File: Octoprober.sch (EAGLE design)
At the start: 70 parts, among them J1 10118193-0001LF, P1 TC33X-1, SW1 101-0134-EV, U1 P8X32A-M44, U10 MAX31855KASA+, U11 MAX31855KASA+, U12 MAX31855KASA+, U13 MAX31855KASA+, U14 MAX31855KASA+, U2 CAT24C512WI-GT3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

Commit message: Added lithium battery. Still need to add charger.
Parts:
- removed R14: 1K, PP_Passives:RESISTOR0402
- removed U5: TPS2115ADRBR, PP_PowerIC:TPS2115SON-8
- added BATT1: 1042, PP_Connectors:LI-ION_18650_HOLDER1042
- U3: value TS2937CW33 -> ADP3338AKCZ-3.3-RL; device PP_PowerIC:FIXED_VOLTAGE_REGSOT-223 -> PP_PowerIC:FIXED_VOLTAGE_REGSOT-223_ALT
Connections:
- removed net 5V: C7.1, C9.1, U3.IN, U5.OUT
- removed net ILIM: R14.1, U5.ILIM
- removed net VBUS_2: U5.IN2
- net 3.3V: no longer R13.1
- net GND: now also BATT1.-; no longer R14.2, U5.D1, U5.GND
- net VBATT: now also BATT1.+, C7.1, C9.1, U3.IN; no longer U5.IN1
- net VBUS_P1: no longer R12.1
- net VBUS_P2: now also R12.1, R13.1

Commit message: Added BQ24075RGTT for charging.
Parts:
- added C31, C32, C33: 10uF, PP_Passives:CAPACITOR_NON_POLAR1206
- added R14, R19, R20: 10K, PP_Passives:RESISTOR0402
- added R17: 1.18K, PP_Passives:RESISTOR0402
- added R18: 1.13K, PP_Passives:RESISTOR0402
- added U5: BQ24075RGTT, PP_PowerIC:BQ2407XQFN-16
- R15: value 100K -> 10K
- R16: value 1K -> 10K
- U6: value IRLML6401TRPBF -> 74HC2G04GV,125; device PP_DiscreteSemi:MOSFET_P-CHANNEL_SINGLESOT-23 -> PP_DigitalIC:74HCT2G04GV,125TTSOP-6
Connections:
- net VBUS renamed USB_V0
- removed net P19: U1.P19
- removed net P20: U1.P20
- removed net PWREN_GATE: R15.2, R16.2, U6.GATE
- removed net VBUS_P1: C13.1, C14.1, L1.2, R15.1, U4.VCC, U6.SOURCE
- removed net VBUS_P2: R12.1, R13.1, U6.DRAIN
- new net !PWREN: U5.EN1, U6.2Y
- new net !SLEEP: U1.P20, U5.!CE, U6.1Y
- new net BCD_CHARGER: R20.2, U4.CBUS2, U5.EN2
- new net CHARGING: R15.2, U1.P19, U5.!CHG
- new net ILM: R17.1, U5.ILM
- new net ISET: R18.1, U5.ISET
- new net PGOOD: R16.2, U5.!PGOOD
- new net SLEEP: U4.CBUS1, U6.1A
- new net SYS_V: C32.1, C7.1, C9.1, U3.IN, U5.OUT
- new net TS: R14.1, U5.TS
- new net USB_V1: C13.1, C14.1, C33.1, L1.2, R12.1, R13.1, U4.VCC, U5.IN
- net 3.3V: now also R15.1, R16.1, R19.2, U6.VCC
- net GND: now also C31.2, C32.2, C33.2, R14.2, R17.2, R18.2, R20.1, U5.SYSOFF, U5.VSS, U6.GND
- net PWREN: now also R19.1, U6.2A; no longer R16.1
- net TXRX_LED: now also U4.CBUS0; no longer U4.CBUS2
- net VBATT: now also C31.1, U5.BAT; no longer C7.1, C9.1, U3.IN
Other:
- moved on the sheet: BATT1, R15, R16

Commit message: Still need Battery Monitoring Solution
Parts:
- added U15: BSS138, PP_DiscreteSemi:MOSFET_N-CHANNEL_SINGLESOT-23
- LCD1: device PP_Displays:CHAR_DISPLAY1602_4_HOLE -> PP_Displays:HD44780_LCD1602_COUNTERSINK
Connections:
- removed net N$38: LCD1.BK_V
- removed net N$39: LCD1.BK_GND
- removed net P21: U1.P21
- new net BK_GATE: U1.P21, U15.GATE
- new net BK_GND: LCD1.BK_GND, U15.DRAIN
- new net SYS_V_SW: C7.1, C9.1, U3.IN
- net !PWREN: now also R19.1, U4.CBUS3, U6.2A; no longer U5.EN1, U6.2Y
- net !SLEEP: now also U4.CBUS1, U6.1A; no longer U5.!CE, U6.1Y
- net 3.3V: now also LCD1.BK_V
- net GND: now also U15.SOURCE
- net PWREN: now also U5.EN1, U6.2Y; no longer R19.1, U4.CBUS3, U6.2A
- net SLEEP: now also U5.!CE, U6.1Y; no longer U4.CBUS1, U6.1A
- net SYS_V: no longer C7.1, C9.1, U3.IN
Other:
- moved on the sheet: BATT1, C10, C2, C3, C31, C32, C33, C4, C5, C6, C7, C8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

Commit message: Added Soft power switch
Soft power circuit to enable MCU to initiate a shutdown of the system to
prevent corruption of the SD Card.
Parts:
- added C34, C35: 0.1uF, PP_Passives:CAPACITOR_NON_POLAR0402
- added C36: 10uF, PP_Passives:CAPACITOR_NON_POLAR1206
- added D3: PMEG6030EP,115, PP_Passives:DIODESOD-128
- added R21, R22, R23, R25: 10K, PP_Passives:RESISTOR0402
- added R24, R26: 100K, PP_Passives:RESISTOR0402
- added R27: 300K, PP_Passives:RESISTOR0402
- added SW2, SW3, SW4, SW5: EVQ-Q2203W, PP_Electromechanical:SPSTEVQ-Q2203W
- added U16: PMV22EN,215, PP_DiscreteSemi:MOSFET_N-CHANNEL_SINGLESOT-23
- added U17: PMV160UP,215, PP_DiscreteSemi:MOSFET_P-CHANNEL_SINGLESOT-23
- SW1: value 101-0134-EV -> EVQ-Q2203W; device PP_Electromechanical:SPST101-0134-EV -> PP_Electromechanical:SPSTEVQ-Q2203W
- U15: value BSS138 -> PMV22EN,215
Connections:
- removed net P22: U1.P22
- removed net P23: U1.P23
- removed net P24: U1.P24
- removed net P25: U1.P25
- new net N$4: C35.1, D3.CATHODE, R25.1, SW5.B
- new net N$5: C36.2, R27.2, U16.GATE
- new net PWR_SW: D3.ANODE, R26.1, R27.1, U1.P25
- new net SW_DWN: R23.1, SW4.B, U1.P24
- new net SW_SEL: R22.1, SW3.B, U1.P23
- new net SW_UP: R21.1, SW2.B, U1.P22
- new net S_P_G: C34.2, C35.2, R24.1, U16.DRAIN, U17.GATE
- net 3.3V: now also C36.1, R21.2, R22.2, R23.2, R26.2
- net GND: now also SW2.A, SW3.A, SW4.A, SW5.A, U16.SOURCE
- net SYS_V: now also C34.1, R24.2, R25.2, U17.SOURCE
- net SYS_V_SW: now also U17.DRAIN
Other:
- moved on the sheet: J1

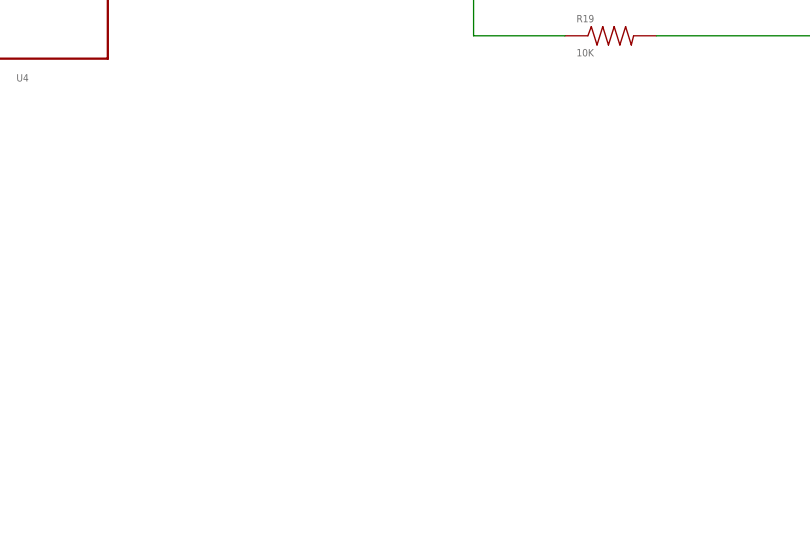
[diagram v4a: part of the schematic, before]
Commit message: Added ADC. Might use it for battery voltage level.
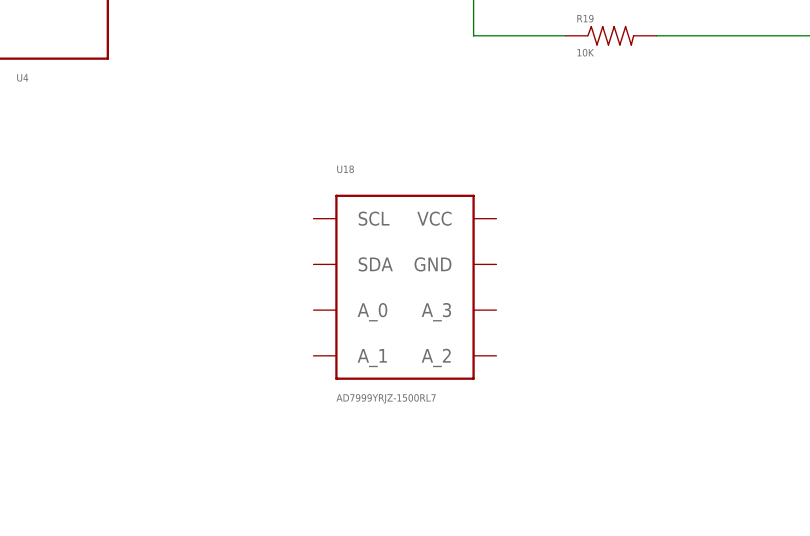
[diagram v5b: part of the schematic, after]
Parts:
- added U18: AD7999YRJZ-1500RL7, PP_DigitalIC:AD799XSOT-23-8
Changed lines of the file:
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@@
 <part name="R26" library="PP_Passives" deviceset="RESISTOR" device="0402" value="100K"/>
 <part name="R27" library="PP_Passives" deviceset="RESISTOR" device="0402" value="300K"/>
+<part name="U18" library="PP_DigitalIC" deviceset="AD799X" device="SOT-23-8" value="AD7999YRJZ-1500RL7"/>
 </parts>
 <sheets>
@@
 <instance part="R26" gate="G$1" x="139.7" y="-66.04" rot="R90"/>
 <instance part="R27" gate="G$1" x="132.08" y="-76.2" rot="R180"/>
+<instance part="U18" gate="G$1" x="-15.24" y="-101.6"/>
 </instances>
 <busses>

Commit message: Created Board. Still need to figure out connector
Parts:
- added U$2: OCTOPROBER_LOGONORMAL, PP_Aesthetics:OCTOPROBER_LOGONORMAL
- U1: device PP_DigitalIC:P8X32A_PROPELLERQFN-44 -> PP_DigitalIC:P8X32A_PROPELLERLQFP/QFN-44
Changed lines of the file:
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@@
 <grid distance="0.1" unitdist="inch" unit="inch" style="lines" multiple="1" display="no" altdistance="0.01" altunitdist="inch" altunit="inch"/>
 <layers>
-<layer number="1" name="Top" color="4" fill="1" visible="no" active="no"/>
-<layer number="16" name="Bottom" color="1" fill="1" visible="no" active="no"/>
-<layer number="17" name="Pads" color="2" fill="1" visible="no" active="no"/>
-<layer number="18" name="Vias" color="2" fill="1" visible="no" active="no"/>
-<layer number="19" name="Unrouted" color="6" fill="1" visible="no" active="no"/>
-<layer number="20" name="Dimension" color="15" fill="1" visible="no" active="no"/>
-<layer number="21" name="tPlace" color="7" fill="1" visible="no" active="no"/>
-<layer number="22" name="bPlace" color="7" fill="1" visible="no" active="no"/>
-<layer number="23" name="tOrigins" color="15" fill="1" visible="no" active="no"/>
-<layer number="24" name="bOrigins" color="15" fill="1" visible="no" active="no"/>
-<layer number="25" name="tNames" color="7" fill="1" visible="no" active="no"/>
-<layer number="26" name="bNames" color="7" fill="1" visible="no" active="no"/>
-<layer number="27" name="tValues" color="7" fill="1" visible="no" active="no"/>
-<layer number="28" name="bValues" color="7" fill="1" visible="no" active="no"/>
+<layer number="1" name="Top" color="4" fill="1" visible="yes" active="no"/>
+<layer number="16" name="Bottom" color="1" fill="1" visible="yes" active="no"/>
+<layer number="17" name="Pads" color="2" fill="1" visible="yes" active="no"/>
+<layer number="18" name="Vias" color="2" fill="1" visible="yes" active="no"/>
+<layer number="19" name="Unrouted" color="6" fill="1" visible="yes" active="no"/>
+<layer number="20" name="Dimension" color="15" fill="1" visible="yes" active="no"/>
+<layer number="21" name="tPlace" color="7" fill="1" visible="yes" active="no"/>
+<layer number="22" name="bPlace" color="7" fill="1" visible="yes" active="no"/>
+<layer number="23" name="tOrigins" color="15" fill="1" visible="yes" active="no"/>
+<layer number="24" name="bOrigins" color="15" fill="1" visible="yes" active="no"/>
+<layer number="25" name="tNames" color="7" fill="1" visible="yes" active="no"/>
+<layer number="26" name="bNames" color="7" fill="1" visible="yes" active="no"/>
+<layer number="27" name="tValues" color="7" fill="1" visible="yes" active="no"/>
+<layer number="28" name="bValues" color="7" fill="1" visible="yes" active="no"/>
 <layer number="29" name="tStop" color="7" fill="3" visible="no" active="no"/>
 <layer number="30" name="bStop" color="7" fill="6" visible="no" active="no"/>
@@
 <layer number="35" name="tGlue" color="7" fill="4" visible="no" active="no"/>
 <layer number="36" name="bGlue" color="7" fill="5" visible="no" active="no"/>
-<layer number="37" name="tTest" color="7" fill="1" visible="no" active="no"/>
-<layer number="38" name="bTest" color="7" fill="1" visible="no" active="no"/>
+<layer number="37" name="tTest" color="7" fill="1" visible="yes" active="no"/>
+<layer number="38" name="bTest" color="7" fill="1" visible="yes" active="no"/>
 <layer number="39" name="tKeepout" color="4" fill="11" visible="no" active="no"/>
 <layer number="40" name="bKeepout" color="1" fill="11" visible="no" active="no"/>
@@
 <layer number="44" name="Drills" color="7" fill="1" visible="no" active="no"/>
 <layer number="45" name="Holes" color="7" fill="1" visible="no" active="no"/>
-<layer number="46" name="Milling" color="3" fill="1" visible="no" active="no"/>
-<layer number="47" name="Measures" color="7" fill="1" visible="no" active="no"/>
-<layer number="48" name="Document" color="7" fill="1" visible="no" active="no"/>
-<layer number="49" name="Reference" color="7" fill="1" visible="no" active="no"/>
-<layer number="50" name="dxf" color="7" fill="1" visible="no" active="no"/>
-<layer number="51" name="tDocu" color="7" fill="1" visible="no" active="no"/>
-<layer number="52" name="bDocu" color="7" fill="1" visible="no" active="no"/>
-<layer number="53" name="tGND_GNDA" color="7" fill="9" visible="no" active="no"/>
-<layer number="54" name="bGND_GNDA" color="1" fill="9" visible="no" active="no"/>
-<layer number="56" name="wert" color="7" fill="1" visible="no" active="no"/>
+<layer number="46" name="Milling" color="3" fill="1" visible="yes" active="no"/>
+<layer number="47" name="Measures" color="7" fill="1" visible="yes" active="no"/>
+<layer number="48" name="Document" color="7" fill="1" visible="yes" active="no"/>
+<layer number="49" name="Reference" color="7" fill="1" visible="yes" active="no"/>
+<layer number="50" name="dxf" color="7" fill="1" visible="yes" active="no"/>
+<layer number="51" name="tDocu" color="7" fill="1" visible="yes" active="no"/>
+<layer number="52" name="bDocu" color="7" fill="1" visible="yes" active="no"/>
+<layer number="53" name="tGND_GNDA" color="7" fill="9" visible="yes" active="no"/>
+<layer number="54" name="bGND_GNDA" color="1" fill="9" visible="yes" active="no"/>
+<layer number="56" name="wert" color="7" fill="1" visible="yes" active="no"/>
 <layer number="91" name="Nets" color="2" fill="1" visible="yes" active="yes"/>
 <layer number="92" name="Busses" color="1" fill="1" visible="yes" active="yes"/>
@@
 </classes>
 <parts>
-<part name="U1" library="PP_DigitalIC" deviceset="P8X32A_PROPELLER" device="QFN-44" value="P8X32A-M44"/>
+<part name="U1" library="PP_DigitalIC" deviceset="P8X32A_PROPELLER" device="LQFP/QFN-44" value="P8X32A-M44"/>
 <part name="X1" library="PP_FreqCtrl" deviceset="CRYSTAL" device="HC-49" value="ATS060CSM-1"/>
 <part name="R1" library="PP_Passives" deviceset="RESISTOR" device="0402" value="10K"/>
@@
 <part name="R27" library="PP_Passives" deviceset="RESISTOR" device="0402" value="300K"/>
 <part name="U18" library="PP_DigitalIC" deviceset="AD799X" device="SOT-23-8" value="AD7999YRJZ-1500RL7"/>
+<part name="U$2" library="PP_Aesthetics" deviceset="OCTOPROBER_LOGO" device="NORMAL"/>
 </parts>
 <sheets>
@@
 <instance part="R27" gate="G$1" x="132.08" y="-76.2" rot="R180"/>
 <instance part="U18" gate="G$1" x="-15.24" y="-101.6"/>
+<instance part="U$2" gate="G$1" x="-284.48" y="-101.6"/>
 </instances>
 <busses>

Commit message: Worked on the layout some more.
Still need lots of work and connectors.
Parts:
- U1: device PP_DigitalIC:P8X32A_PROPELLERLQFP/QFN-44 -> PP_DigitalIC:P8X32A_PROPELLERQFN-44
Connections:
- removed net P26: U1.P26
- removed net SD_CLK: U1.P2
- net LCD_D4: now also U1.P8; no longer U1.P5
- net LCD_D5: now also U1.P7; no longer U1.P6
- net LCD_D6: now also U1.P6; no longer U1.P7
- net LCD_D7: now also U1.P5; no longer U1.P8
- net LCD_E: now also U1.P26
- net SD_CS: now also U1.P3; no longer U1.P0
- net SD_DI: now also U1.P2; no longer U1.P1
- net SD_DO: now also U1.P0; no longer U1.P3
- net SD_SCLK: now also U1.P1
- net TP_SCK: now also U1.P9; no longer U1.P10
- net TP_SO: now also U1.P10; no longer U1.P9
